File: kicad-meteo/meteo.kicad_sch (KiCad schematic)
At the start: 17 parts, among them J1 BUCK, J2 Connector I2C extension, J3 Solar_Panel, J4 Battery, J5 Battery_Internal, SW1 SW_DIP_x01, U1 DHT11, U2 DS18B20, U4 MOUDLE-SEEEDUINO-XIAO-ESP32C3

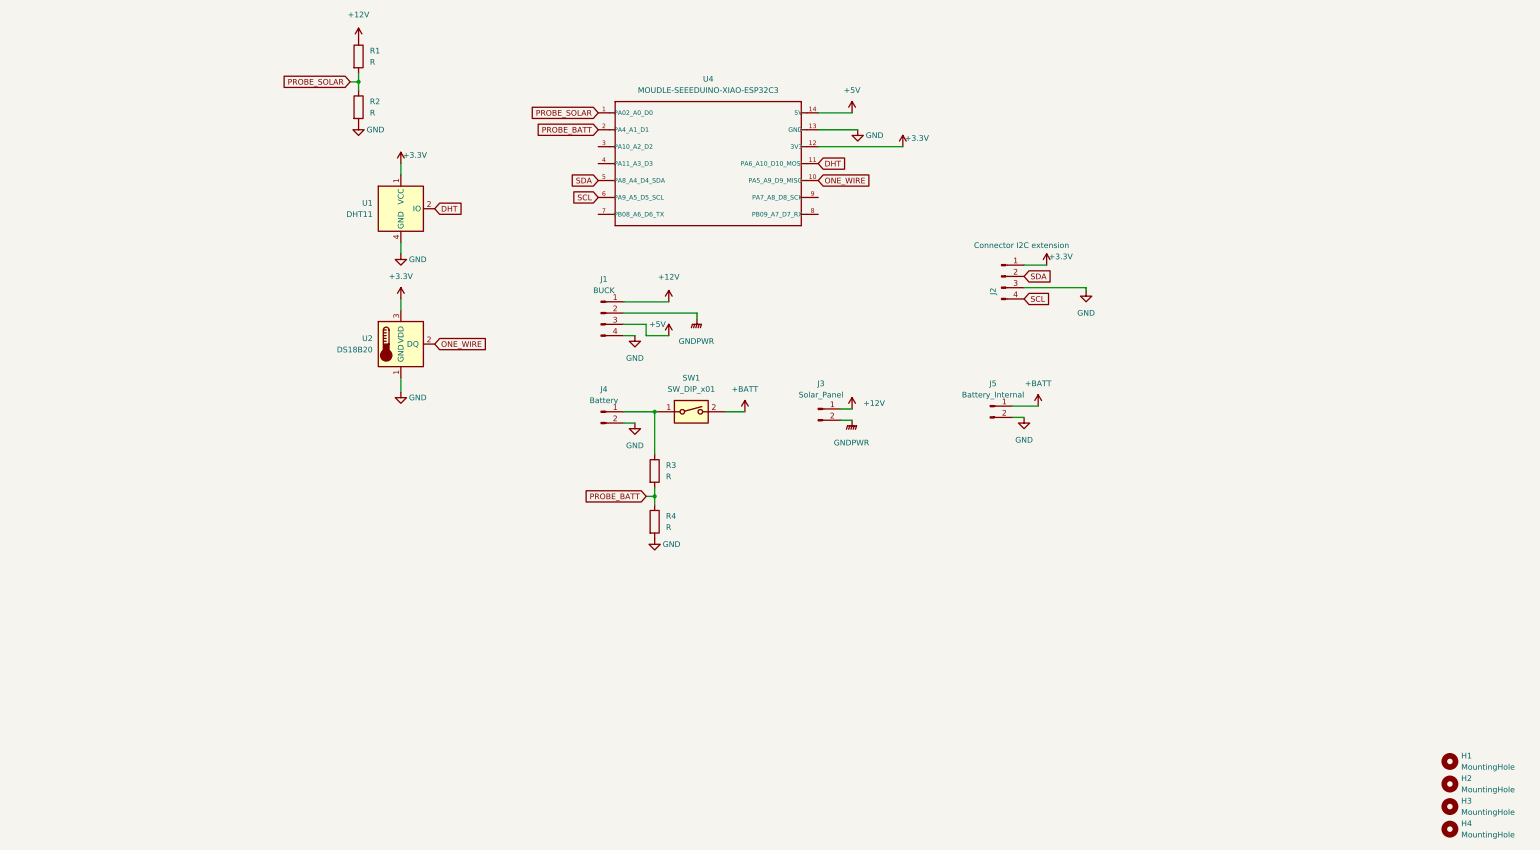
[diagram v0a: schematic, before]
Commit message: feat(meteo): fix pin mapping and add switch, v1.1.0
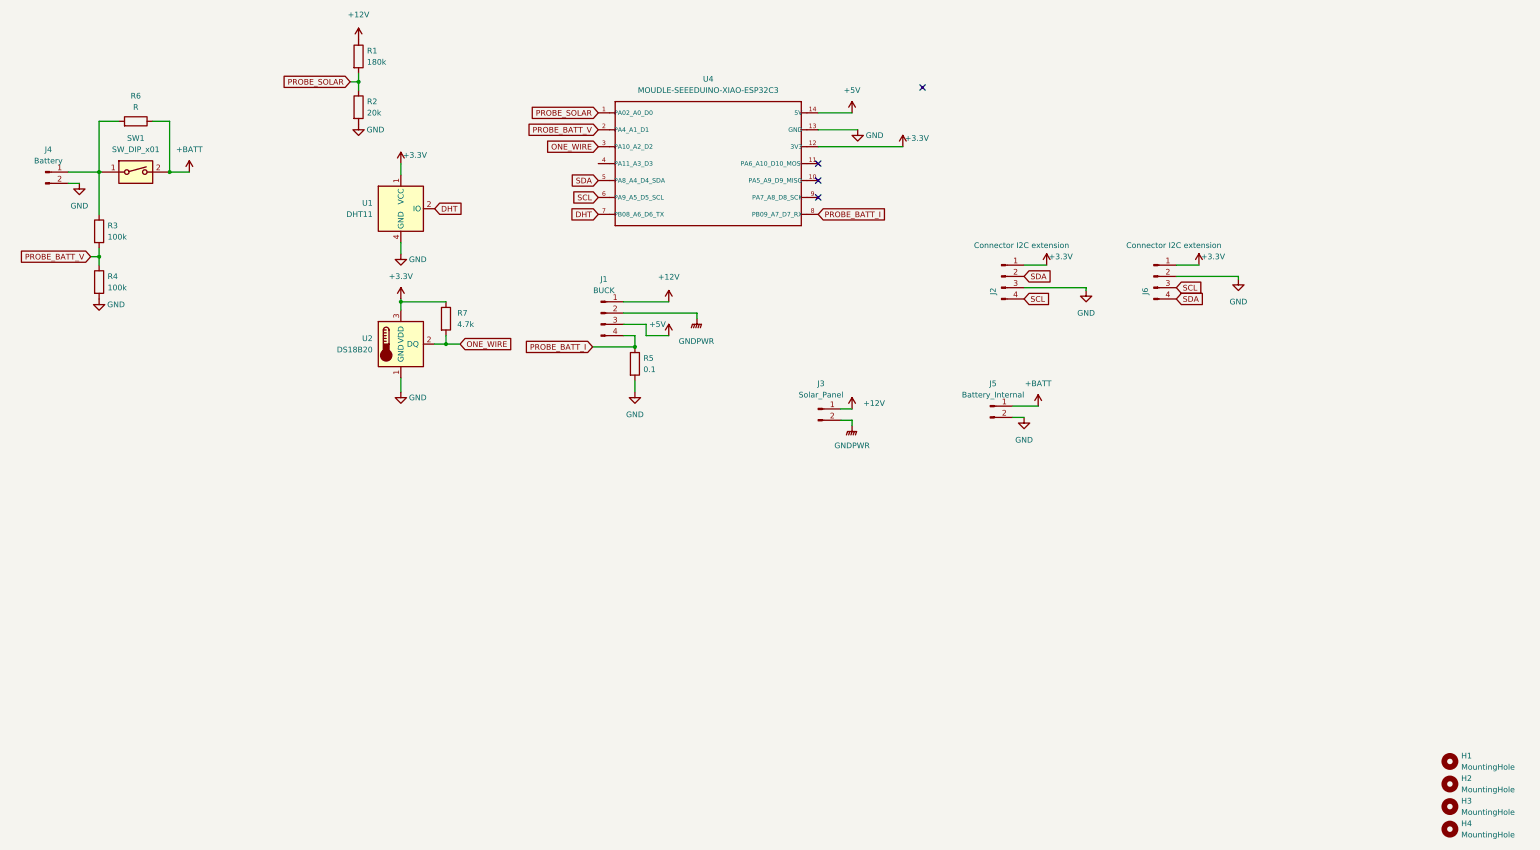
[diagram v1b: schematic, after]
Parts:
- added J6: Connector I2C extension, Connector_PinHeader_2.54mm:PinHeader_1x04_P2.54mm_Vertical, symbol Connector:Conn_01x04_Male
- added R5: 0.1, Resistor_SMD:R_1206_3216Metric_Pad1.30x1.75mm_HandSolder, symbol Device:R
- added R6: R, Resistor_SMD:R_1206_3216Metric_Pad1.30x1.75mm_HandSolder, symbol Device:R
- added R7: 4.7k, Resistor_SMD:R_1206_3216Metric_Pad1.30x1.75mm_HandSolder, symbol Device:R
- R1: value R -> 180k
- R2: value R -> 20k
- R3, R4: value R -> 100k
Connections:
- net +3.3V: now also J6.1 (Pin_1), R7.1
- net +BATT: now also R6.1
- net DHT: now also U4.7 (PB08_A6_D6_TX); no longer U4.11 (PA6_A10_D10_MOSI)
- net GND: now also J6.2 (Pin_2), R5.2; no longer J1.4 (Pin_4)
- net ONE_WIRE: now also U4.3 (PA10_A2_D2), R7.2; no longer U4.10 (PA5_A9_D9_MISO)
- net SCL: now also J6.3 (Pin_3)
- net SDA: now also J6.4 (Pin_4)
- net PROBE_BATT_I: now reaches U4.8 (PB09_A7_D7_RX)
- net PROBE_BATT_I: now also J1.4 (Pin_4), R5.1
- net at J4.1 (Pin_1), R3.1, SW1.1: now also R6.2
- net PROBE_BATT renamed PROBE_BATT_V
- no-connect marks 0 -> 4
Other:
- moved on the sheet: J4, R3, R4, SW1

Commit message: fix: add pull-up for DHT-22
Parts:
- added R8: 4.7k, Resistor_SMD:R_1206_3216Metric_Pad1.30x1.75mm_HandSolder, symbol Device:R
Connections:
- net +3.3V: now also R8.1
- net DHT: now also R8.2
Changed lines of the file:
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@@
   (junction (at 206.375 130.175) (diameter 0) (color 0 0 0 0)
   )
+  (junction (at 165.1 99.06) (diameter 0) (color 0 0 0 0)
+  )
   (junction (at 163.83 129.54) (diameter 0) (color 0 0 0 0)
   )
   (junction (at 144.145 70.485) (diameter 0) (color 0 0 0 0)
+  )
+  (junction (at 153.67 90.805) (diameter 0) (color 0 0 0 0)
   )
   (junction (at 153.67 120.015) (diameter 0) (color 0 0 0 0)
@@
     (stroke (width 0) (type default) (color 0 0 0 0))
   )
-  (wire (pts (xy 153.67 88.9) (xy 153.67 91.44))
+  (wire (pts (xy 153.67 88.9) (xy 153.67 90.805))
     (stroke (width 0) (type default) (color 0 0 0 0))
   )
@@
     (stroke (width 0) (type default) (color 0 0 0 0))
   )
+  (wire (pts (xy 153.67 90.805) (xy 153.67 91.44))
+    (stroke (width 0) (type default) (color 0 0 0 0))
+  )
+  (wire (pts (xy 165.1 90.805) (xy 153.67 90.805))
+    (stroke (width 0) (type default) (color 0 0 0 0))
+  )
   (wire (pts (xy 247.65 85.09) (xy 266.7 85.09))
     (stroke (width 0) (type default) (color 0 0 0 0))
@@
     (stroke (width 0) (type default) (color 0 0 0 0))
   )
+  (wire (pts (xy 161.29 99.06) (xy 165.1 99.06))
+    (stroke (width 0) (type default) (color 0 0 0 0))
+  )
   (wire (pts (xy 161.29 129.54) (xy 163.83 129.54))
     (stroke (width 0) (type default) (color 0 0 0 0))
@@
   )
   (wire (pts (xy 196.85 130.175) (xy 206.375 130.175))
+    (stroke (width 0) (type default) (color 0 0 0 0))
+  )
+  (wire (pts (xy 165.1 99.06) (xy 171.45 99.06))
+    (stroke (width 0) (type default) (color 0 0 0 0))
+  )
+  (wire (pts (xy 165.1 98.425) (xy 165.1 99.06))
     (stroke (width 0) (type default) (color 0 0 0 0))
   )
@@
     )
   )
-  (global_label "DHT" (shape input) (at 161.29 99.06 0) (fields_autoplaced)
+  (global_label "DHT" (shape input) (at 171.45 99.06 0) (fields_autoplaced)
     (effects (font (size 1.27 1.27)) (justify left))
-    (property "Intersheet References" "${INTERSHEET_REFS}" (id 0) (at 167.2712 98.9806 0)
+    (property "Intersheet References" "${INTERSHEET_REFS}" (id 0) (at 177.4312 98.9806 0)
       (effects (font (size 1.27 1.27)) (justify left) hide)
     )
@@
     (pin "1")
   )
+  (symbol (lib_id "Device:R") (at 165.1 94.615 0) (unit 1)
+    (in_bom yes) (on_board yes) (fields_autoplaced)
+    (property "Reference" "R8" (id 0) (at 167.64 93.3449 0)
+      (effects (font (size 1.27 1.27)) (justify left))
+    )
+    (property "Value" "4.7k" (id 1) (at 167.64 95.8849 0)
+      (effects (font (size 1.27 1.27)) (justify left))
+    )
+    (property "Footprint" "Resistor_SMD:R_1206_3216Metric_Pad1.30x1.75mm_HandSolder" (id 2) (at 163.322 94.615 90)
+      (effects (font (size 1.27 1.27)) hide)
+    )
+    (property "Datasheet" "~" (id 3) (at 165.1 94.615 0)
+      (effects (font (size 1.27 1.27)) hide)
+    )
+    (pin "1")
+    (pin "2")
+  )
   (symbol (lib_id "power:+12V") (at 144.145 60.96 0) (unit 1)
     (in_bom yes) (on_board yes) (fields_autoplaced)
@@
       (reference "R7") (unit 1) (value "4.7k") (footprint "Resistor_SMD:R_1206_3216Metric_Pad1.30x1.75mm_HandSolder")
     )
+    (path "/355eb16e-8056-4878-8248-9402cec81545"
+      (reference "R8") (unit 1) (value "4.7k") (footprint "Resistor_SMD:R_1206_3216Metric_Pad1.30x1.75mm_HandSolder")
+    )
     (path "/9c735035-d8f3-4880-8e8b-2a85e2d8e52c"

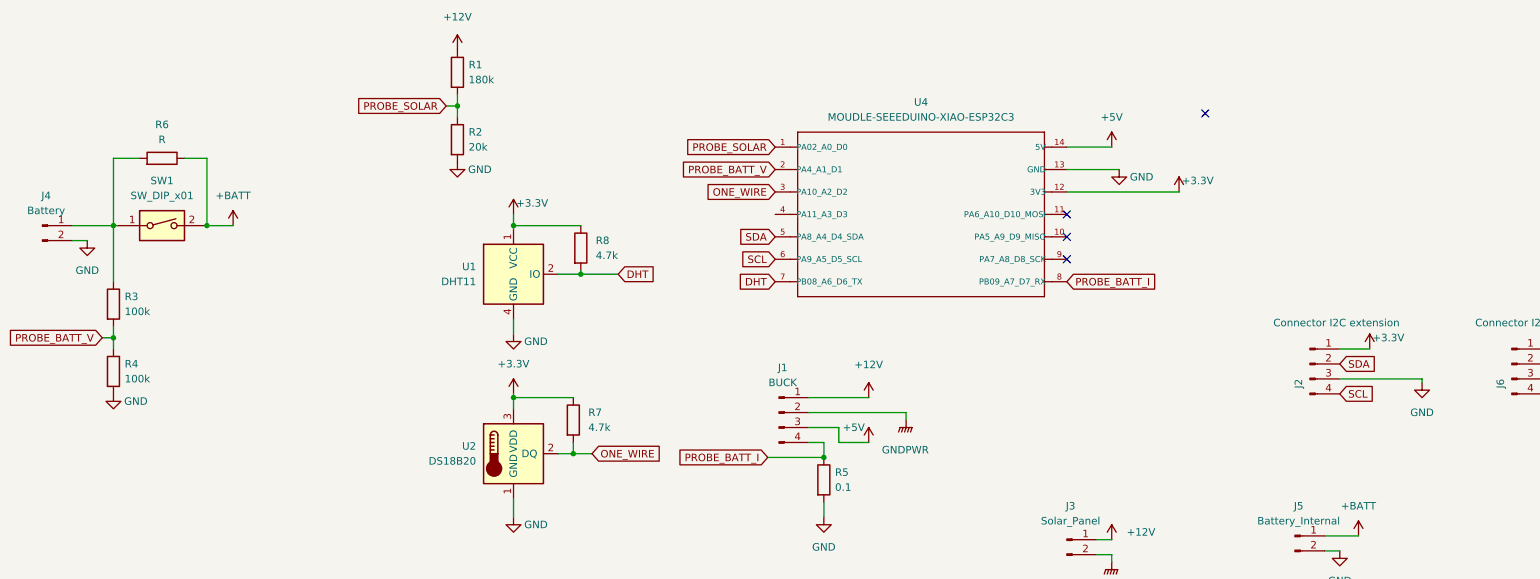
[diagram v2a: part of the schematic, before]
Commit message: fix: correct AD pin for monitoring and ground
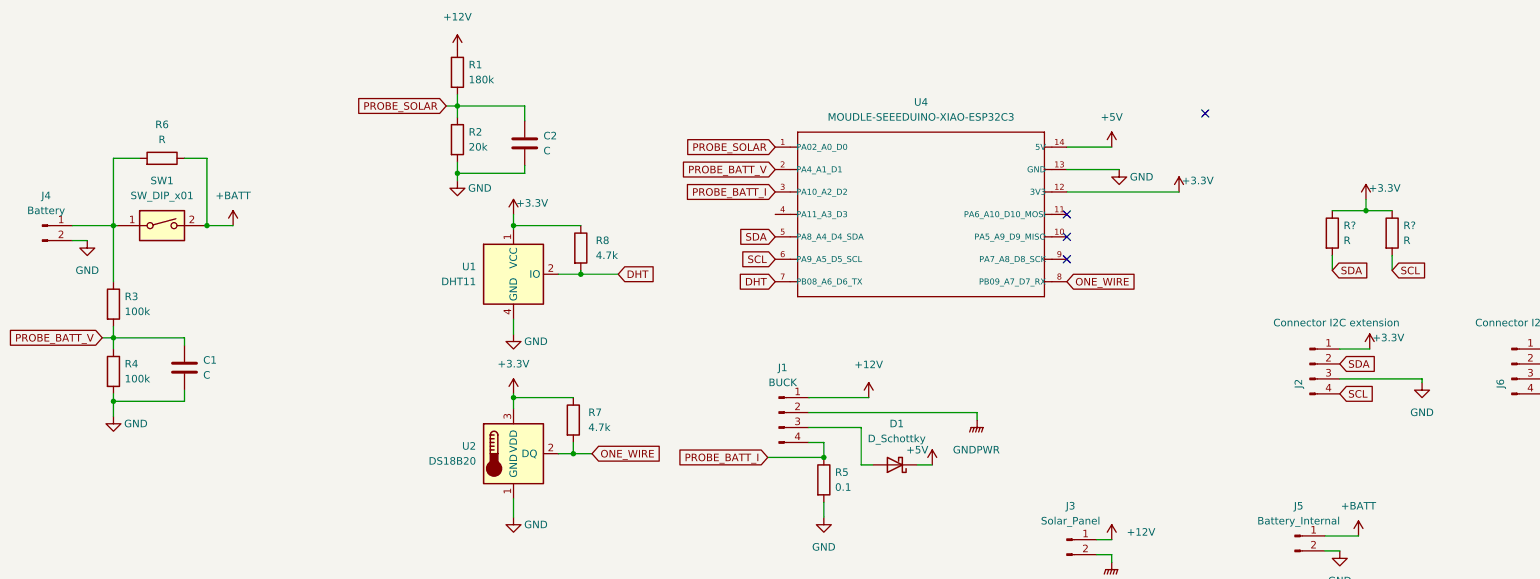
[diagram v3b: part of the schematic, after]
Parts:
- added C1, C2: C, Capacitor_SMD:C_1206_3216Metric_Pad1.33x1.80mm_HandSolder, symbol Device:C
- added D1: D_Schottky, Diode_SMD:D_1206_3216Metric_Pad1.42x1.75mm_HandSolder, symbol Device:D_Schottky
- added R? (x2): R, symbol Device:R
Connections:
- net +3.3V: now also R?.1, R?.1
- net +5V: now also D1.1 (K); no longer J1.3 (Pin_3)
- net GND: now also C1.2, C2.2
- net ONE_WIRE: now also U4.8 (PB09_A7_D7_RX); no longer U4.3 (PA10_A2_D2)
- net PROBE_BATT_I: now also U4.3 (PA10_A2_D2); no longer U4.8 (PB09_A7_D7_RX)
- net PROBE_BATT_V: now also C1.1
- net PROBE_SOLAR: now also C2.1
- net SCL: now also R?.2
- net SDA: now also R?.2
- new net: D1.2 (A), J1.3 (Pin_3)
